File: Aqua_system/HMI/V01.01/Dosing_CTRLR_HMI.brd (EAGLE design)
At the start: 135 x 82 mm, 62 parts, among them IC1 74LS47N, Q1 BC817, Q2 BC817, Q3 BC817, Q4 BC817, X1 MICROMATCH-16

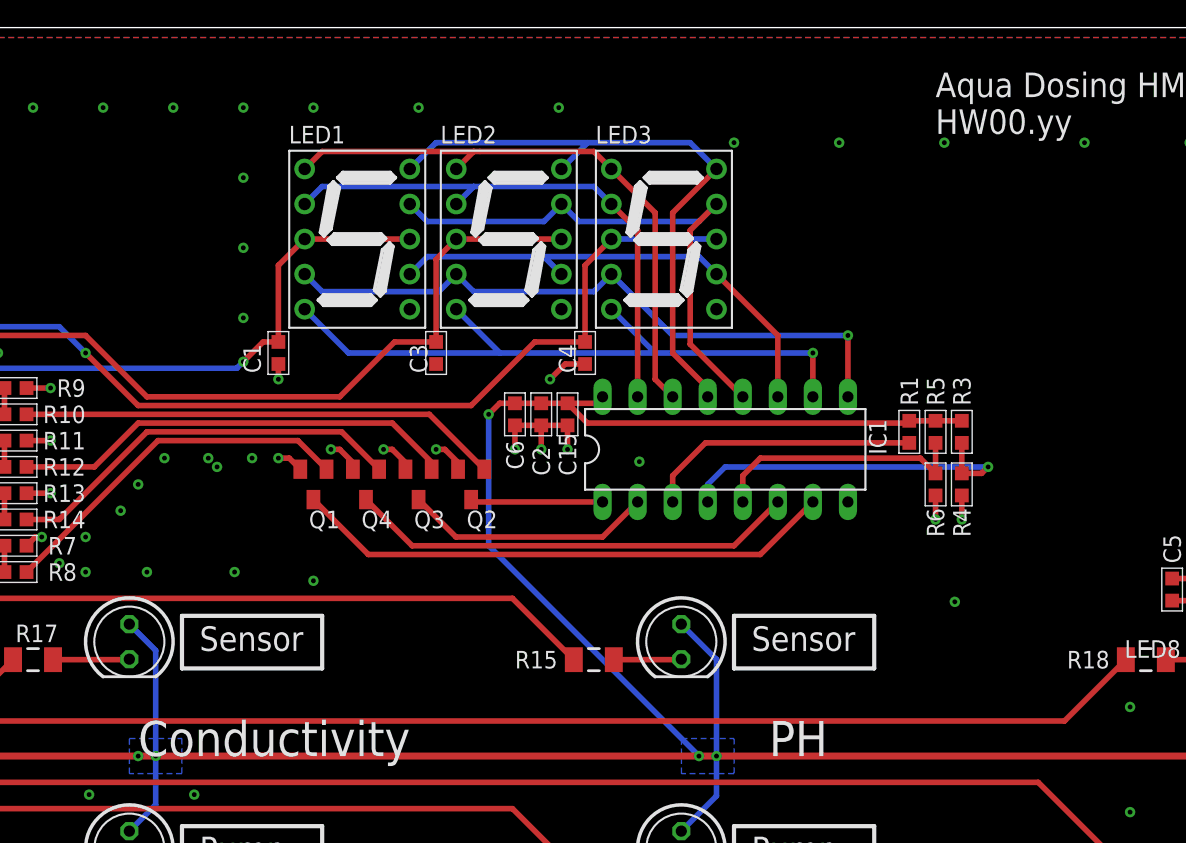
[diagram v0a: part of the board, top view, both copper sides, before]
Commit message: Dosing Controller HMI HW01.01
Minor Changes introduced.
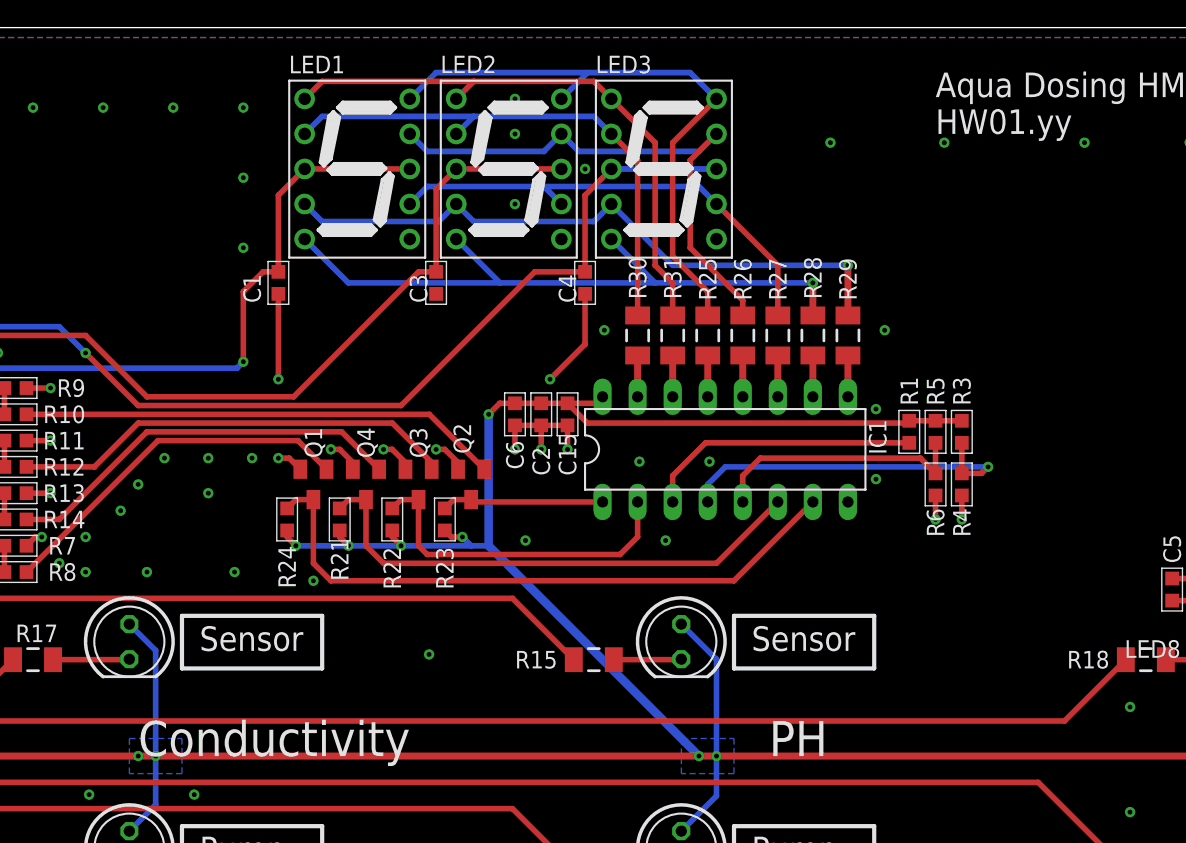
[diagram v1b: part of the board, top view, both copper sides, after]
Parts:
- added R21, R22, R23, R24: 10K 1%, Labops_Lib_AH:EIA0603
- added R25, R26, R27, R28, R29, R30, R31: 150R 1%, Labops_Lib_AH:EIA1206
- moved C1 5.08 mm to (50.8, 63.5)
- moved C3 5.08 mm to (62.2, 63.5)
- moved C4 5.08 mm to (73.0, 63.5)
- moved LED1 5.08 mm to (56.5, 71.8)
- moved LED2 5.08 mm to (67.5, 71.8)
- moved LED3 5.08 mm to (78.7, 71.8)
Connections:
- new net N$12: IC1.13, R25.2
- new net N$27: IC1.12, R26.2
- new net N$28: IC1.11, R27.2
- new net N$29: IC1.10, R28.2
- new net N$30: IC1.9, R29.2
- new net N$31: IC1.15, R30.2
- new net N$32: IC1.14, R31.2
- net N$1: now also R25.1; no longer IC1.13
- net N$19: now also R24.2
- net N$2: now also R26.1; no longer IC1.12
- net N$20: now also R23.2
- net N$21: now also R22.2
- net N$22: now also R21.2
- net N$3: now also R27.1; no longer IC1.11
- net N$4: now also R28.1; no longer IC1.10
- net N$5: now also R29.1; no longer IC1.9
- net N$6: now also R30.1; no longer IC1.15
- net N$7: now also R31.1; no longer IC1.14
- net VCC: now also R21.1, R22.1, R23.1, R24.1
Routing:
- net VCC: track 262.6 -> 283.0 mm, vias 5 -> 9
- net GND: track 55.5 -> 64.8 mm, vias 141 -> 147
- net N$21: track 18.0 -> 24.7 mm
- net N$19: track 39.4 -> 45.9 mm
- net N$22: track 32.5 -> 37.7 mm
- net VCC_DISPLAY_1: track 94.7 -> 99.7 mm
- net N$32: track 0.00 -> 3.00 mm
- net N$31: track 0.00 -> 3.00 mm
- net N$29: track 0.00 -> 3.00 mm
- net N$27: track 0.00 -> 3.00 mm
- net N$30: track 0.00 -> 3.00 mm
- net N$28: track 0.00 -> 3.00 mm
- net N$12: track 0.00 -> 3.00 mm
- net N$20: track 9.60 -> 11.8 mm
- net VCC_DISPLAY_3: track 126.7 -> 128.8 mm
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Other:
- board text added: "Aqua Dosing HMI HW01.yy"
- board text removed: "Aqua Dosing HMI HW00.yy"

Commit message: HW02.02
Improvements after HW Functional Testing
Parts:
- R15, R16, R17, R18, R19, R2, R20: value R_1206EIA1206 -> 22R 1%
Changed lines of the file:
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@@
 <attribute name="VALUE" x="78.1966" y="19.2996" locked="yes" size="1.27" layer="27" ratio="10" rot="R270"/>
 </element>
-<element name="R2" library="Labops_Lib_AH" package="EIA1206" value="R_1206EIA1206" x="73.66" y="20.955" smashed="yes">
+<element name="R2" library="Labops_Lib_AH" package="EIA1206" value="22R 1%" x="73.66" y="20.955" smashed="yes">
 <attribute name="DESCRIPTION" value="" x="73.66" y="20.955" size="1.778" layer="27" display="off"/>
 <attribute name="MFN" value="Open Source R1206" x="73.66" y="20.955" size="1.778" layer="27" display="off"/>
@@
 <attribute name="VALUE" x="71.501" y="17.78" size="1.27" layer="27" font="vector" rot="R270" display="off"/>
 </element>
-<element name="R15" library="Labops_Lib_AH" package="EIA1206" value="R_1206EIA1206" x="73.66" y="36.195" smashed="yes">
+<element name="R15" library="Labops_Lib_AH" package="EIA1206" value="22R 1%" x="73.66" y="36.195" smashed="yes">
 <attribute name="DESCRIPTION" value="" x="73.66" y="36.195" size="1.778" layer="27" display="off"/>
 <attribute name="MFN" value="Open Source R1206" x="73.66" y="36.195" size="1.778" layer="27" display="off"/>
@@
 <attribute name="VALUE" x="73.66" y="34.671" size="1.27" layer="27" font="vector" display="off"/>
 </element>
-<element name="R16" library="Labops_Lib_AH" package="EIA1206" value="R_1206EIA1206" x="33.02" y="21.59" smashed="yes">
+<element name="R16" library="Labops_Lib_AH" package="EIA1206" value="22R 1%" x="33.02" y="21.59" smashed="yes">
 <attribute name="DESCRIPTION" value="" x="33.02" y="21.59" size="1.778" layer="27" display="off"/>
 <attribute name="MFN" value="Open Source R1206" x="33.02" y="21.59" size="1.778" layer="27" display="off"/>
@@
 <attribute name="VALUE" x="29.845" y="16.891" size="1.27" layer="27" font="vector" display="off"/>
 </element>
-<element name="R17" library="Labops_Lib_AH" package="EIA1206" value="R_1206EIA1206" x="33.02" y="36.195" smashed="yes">
+<element name="R17" library="Labops_Lib_AH" package="EIA1206" value="22R 1%" x="33.02" y="36.195" smashed="yes">
 <attribute name="DESCRIPTION" value="" x="33.02" y="36.195" size="1.778" layer="27" display="off"/>
 <attribute name="MFN" value="Open Source R1206" x="33.02" y="36.195" size="1.778" layer="27" display="off"/>
@@
 <attribute name="VALUE" x="33.02" y="34.671" size="1.27" layer="27" font="vector" display="off"/>
 </element>
-<element name="R18" library="Labops_Lib_AH" package="EIA1206" value="R_1206EIA1206" x="113.665" y="36.195" smashed="yes">
+<element name="R18" library="Labops_Lib_AH" package="EIA1206" value="22R 1%" x="113.665" y="36.195" smashed="yes">
 <attribute name="DESCRIPTION" value="" x="113.665" y="36.195" size="1.778" layer="27" display="off"/>
 <attribute name="MFN" value="Open Source R1206" x="113.665" y="36.195" size="1.778" layer="27" display="off"/>
@@
 <attribute name="VALUE" x="106.68" y="33.401" size="1.27" layer="27" font="vector" display="off"/>
 </element>
-<element name="R19" library="Labops_Lib_AH" package="EIA1206" value="R_1206EIA1206" x="113.665" y="20.955" smashed="yes">
+<element name="R19" library="Labops_Lib_AH" package="EIA1206" value="22R 1%" x="113.665" y="20.955" smashed="yes">
 <attribute name="DESCRIPTION" value="" x="113.665" y="20.955" size="1.778" layer="27" display="off"/>
 <attribute name="MFN" value="Open Source R1206" x="113.665" y="20.955" size="1.778" layer="27" display="off"/>
@@
 <attribute name="VALUE" x="106.68" y="18.161" size="1.27" layer="27" font="vector" display="off"/>
 </element>
-<element name="R20" library="Labops_Lib_AH" package="EIA1206" value="R_1206EIA1206" x="113.665" y="6.35" smashed="yes">
+<element name="R20" library="Labops_Lib_AH" package="EIA1206" value="22R 1%" x="113.665" y="6.35" smashed="yes">
 <attribute name="DESCRIPTION" value="" x="113.665" y="6.35" size="1.778" layer="27" display="off"/>
 <attribute name="MFN" value="Open Source R1206" x="113.665" y="6.35" size="1.778" layer="27" display="off"/>
